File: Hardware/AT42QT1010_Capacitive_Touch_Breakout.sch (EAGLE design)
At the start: 28 parts, among them Q1 NPN, U1 AT42QT1010SOT23

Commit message: Ready for red board review
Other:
- note added: "10"
- note removed: "02"
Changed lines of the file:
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@@
 <setting verticaltext="up"/>
 </settings>
-<grid distance="0.1" unitdist="inch" unit="inch" style="lines" multiple="1" display="yes" altdistance="0.01" altunitdist="inch" altunit="inch"/>
+<grid distance="0.1" unitdist="inch" unit="inch" style="lines" multiple="1" display="no" altdistance="0.01" altunitdist="inch" altunit="inch"/>
 <layers>
 <layer number="1" name="Top" color="4" fill="1" visible="no" active="no"/>
@@
 <plain>
 <text x="172.212" y="7.62" size="3.81" layer="94">Shawn Hymel</text>
-<text x="239.014" y="6.604" size="3.81" layer="94">02</text>
+<text x="239.014" y="6.604" size="3.81" layer="94">10</text>
 <wire x1="101.6" y1="185.42" x2="101.6" y2="139.7" width="0.1524" layer="97" style="longdash"/>
 <wire x1="101.6" y1="139.7" x2="101.6" y2="76.2" width="0.1524" layer="97" style="longdash"/>

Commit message: Replaced old IC package with new smaller package
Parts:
- U1: value AT42QT1010SOT23 -> AT42QT1010UDFN; device SparkFun-DigitalIC:AT42QT1010SOT23 -> Testing:AT42QT1010UDFN
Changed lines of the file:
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@@
 <?xml version="1.0" encoding="utf-8"?>
 <!DOCTYPE eagle SYSTEM "eagle.dtd">
-<eagle version="6.0">
+<eagle version="7.7.0">
 <drawing>
 <settings>
@@
 <layer number="54" name="bGND_GNDA" color="1" fill="9" visible="no" active="no"/>
 <layer number="56" name="wert" color="7" fill="1" visible="no" active="no"/>
+<layer number="57" name="tCAD" color="7" fill="1" visible="no" active="no"/>
+<layer number="59" name="tCarbon" color="7" fill="1" visible="no" active="no"/>
+<layer number="60" name="bCarbon" color="7" fill="1" visible="no" active="no"/>
+<layer number="90" name="Modules" color="5" fill="1" visible="no" active="no"/>
 <layer number="91" name="Nets" color="2" fill="1" visible="yes" active="yes"/>
 <layer number="92" name="Busses" color="1" fill="1" visible="yes" active="yes"/>
@@
 <layer number="97" name="Info" color="7" fill="1" visible="yes" active="yes"/>
 <layer number="98" name="Guide" color="6" fill="1" visible="yes" active="yes"/>
+<layer number="99" name="SpiceOrder" color="7" fill="1" visible="yes" active="yes"/>
 <layer number="100" name="Muster" color="7" fill="1" visible="no" active="no"/>
 <layer number="101" name="Patch_Top" color="12" fill="4" visible="yes" active="yes"/>
@@
 <layer number="108" name="tplace-old" color="10" fill="1" visible="yes" active="yes"/>
 <layer number="109" name="ref-old" color="11" fill="1" visible="yes" active="yes"/>
+<layer number="110" name="fp0" color="7" fill="1" visible="yes" active="yes"/>
+<layer number="111" name="LPC17xx" color="7" fill="1" visible="yes" active="yes"/>
+<layer number="112" name="tSilk" color="7" fill="1" visible="yes" active="yes"/>
+<layer number="113" name="IDFDebug" color="4" fill="1" visible="yes" active="yes"/>
+<layer number="114" name="Badge_Outline" color="11" fill="1" visible="no" active="no"/>
+<layer number="115" name="ReferenceISLANDS" color="7" fill="1" visible="yes" active="yes"/>
 <layer number="116" name="Patch_BOT" color="9" fill="4" visible="yes" active="yes"/>
+<layer number="118" name="Rect_Pads" color="7" fill="1" visible="yes" active="yes"/>
 <layer number="121" name="_tsilk" color="7" fill="1" visible="yes" active="yes"/>
 <layer number="122" name="_bsilk" color="7" fill="1" visible="yes" active="yes"/>
+<layer number="123" name="tTestmark" color="7" fill="1" visible="yes" active="yes"/>
+<layer number="124" name="bTestmark" color="7" fill="1" visible="yes" active="yes"/>
 <layer number="125" name="_tNames" color="7" fill="1" visible="yes" active="yes"/>
+<layer number="126" name="_bNames" color="7" fill="1" visible="yes" active="yes"/>
+<layer number="127" name="_tValues" color="7" fill="1" visible="yes" active="yes"/>
+<layer number="128" name="_bValues" color="7" fill="1" visible="yes" active="yes"/>
+<layer number="129" name="Mask" color="7" fill="1" visible="yes" active="yes"/>
+<layer number="131" name="tAdjust" color="7" fill="1" visible="yes" active="yes"/>
+<layer number="132" name="bAdjust" color="7" fill="1" visible="yes" active="yes"/>
 <layer number="144" name="Drill_legend" color="7" fill="1" visible="yes" active="yes"/>
+<layer number="150" name="Notes" color="7" fill="1" visible="yes" active="yes"/>
 <layer number="151" name="HeatSink" color="7" fill="1" visible="yes" active="yes"/>
+<layer number="152" name="_bDocu" color="7" fill="1" visible="yes" active="yes"/>
+<layer number="153" name="FabDoc1" color="7" fill="1" visible="yes" active="yes"/>
+<layer number="154" name="FabDoc2" color="7" fill="1" visible="yes" active="yes"/>
+<layer number="155" name="FabDoc3" color="7" fill="1" visible="yes" active="yes"/>
 <layer number="199" name="Contour" color="7" fill="1" visible="yes" active="yes"/>
 <layer number="200" name="200bmp" color="1" fill="10" visible="yes" active="yes"/>
@@
 <layer number="223" name="223bmp" color="24" fill="1" visible="no" active="no"/>
 <layer number="224" name="224bmp" color="25" fill="1" visible="no" active="no"/>
+<layer number="225" name="225bmp" color="7" fill="1" visible="yes" active="yes"/>
+<layer number="226" name="226bmp" color="7" fill="1" visible="yes" active="yes"/>
+<layer number="227" name="227bmp" color="7" fill="1" visible="yes" active="yes"/>
+<layer number="228" name="228bmp" color="7" fill="1" visible="yes" active="yes"/>
+<layer number="229" name="229bmp" color="7" fill="1" visible="yes" active="yes"/>
+<layer number="230" name="230bmp" color="7" fill="1" visible="yes" active="yes"/>
+<layer number="231" name="231bmp" color="7" fill="1" visible="yes" active="yes"/>
+<layer number="232" name="Eagle3D_PG2" color="7" fill="1" visible="yes" active="yes"/>
+<layer number="233" name="Eagle3D_PG3" color="7" fill="1" visible="yes" active="yes"/>
+<layer number="248" name="Housing" color="7" fill="1" visible="yes" active="yes"/>
+<layer number="249" name="Edge" color="7" fill="1" visible="yes" active="yes"/>
 <layer number="250" name="Descript" color="3" fill="1" visible="no" active="no"/>
 <layer number="251" name="SMDround" color="12" fill="11" visible="no" active="no"/>
 <layer number="254" name="cooling" color="7" fill="1" visible="yes" active="yes"/>
+<layer number="255" name="routoute" color="7" fill="1" visible="yes" active="yes"/>
 </layers>
 <schematic xreflabel="%F%N/%S.%C%R" xrefpart="/%S.%C%R">
@@
 </classes>
 <parts>
-<part name="U1" library="SparkFun-DigitalIC" deviceset="AT42QT1010" device="SOT23"/>
+<part name="U1" library="Testing" deviceset="AT42QT1010" device="UDFN"/>
 <part name="FRAME1" library="SparkFun-Aesthetics" deviceset="FRAME-LETTER" device=""/>
 <part name="LOGO2" library="SparkFun-Aesthetics" deviceset="OSHW-LOGO" device="S"/>

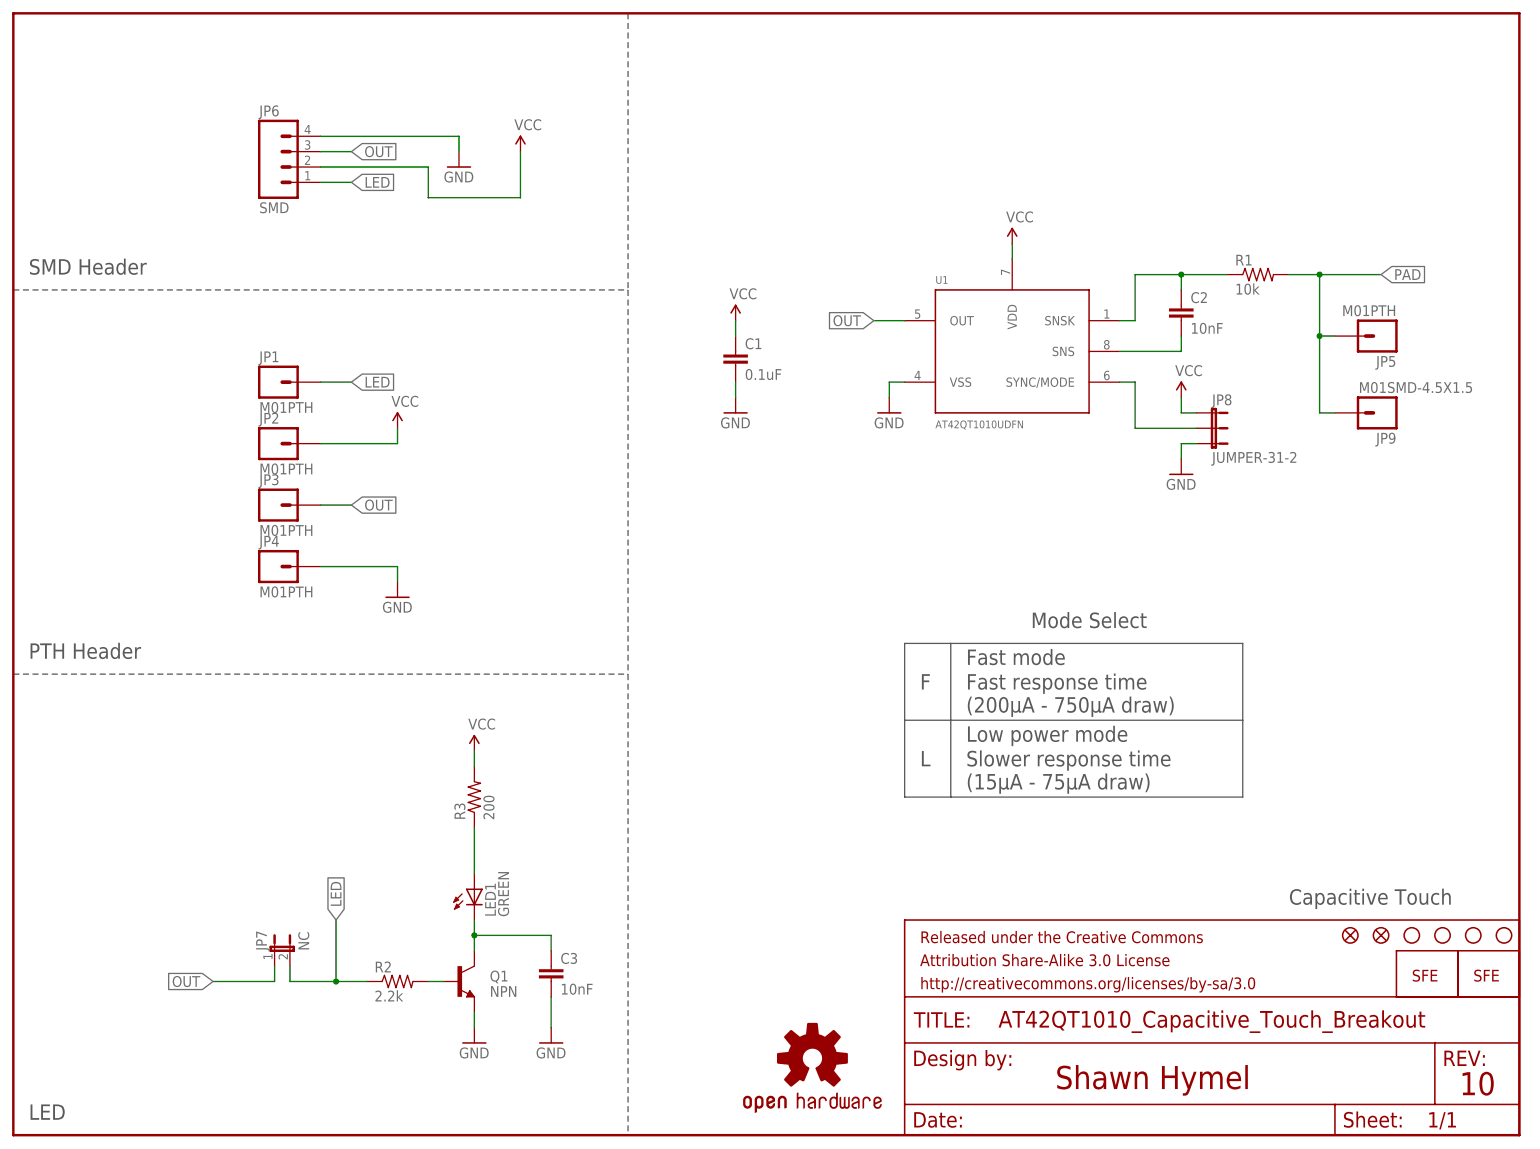
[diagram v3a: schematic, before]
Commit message: Orphans, Schematic changes
Adjusted some traces, updated CC frame, added VCC range, updated jumpers
to a more current package, added fiducials to underside, added Sparkfun
label to schematic.
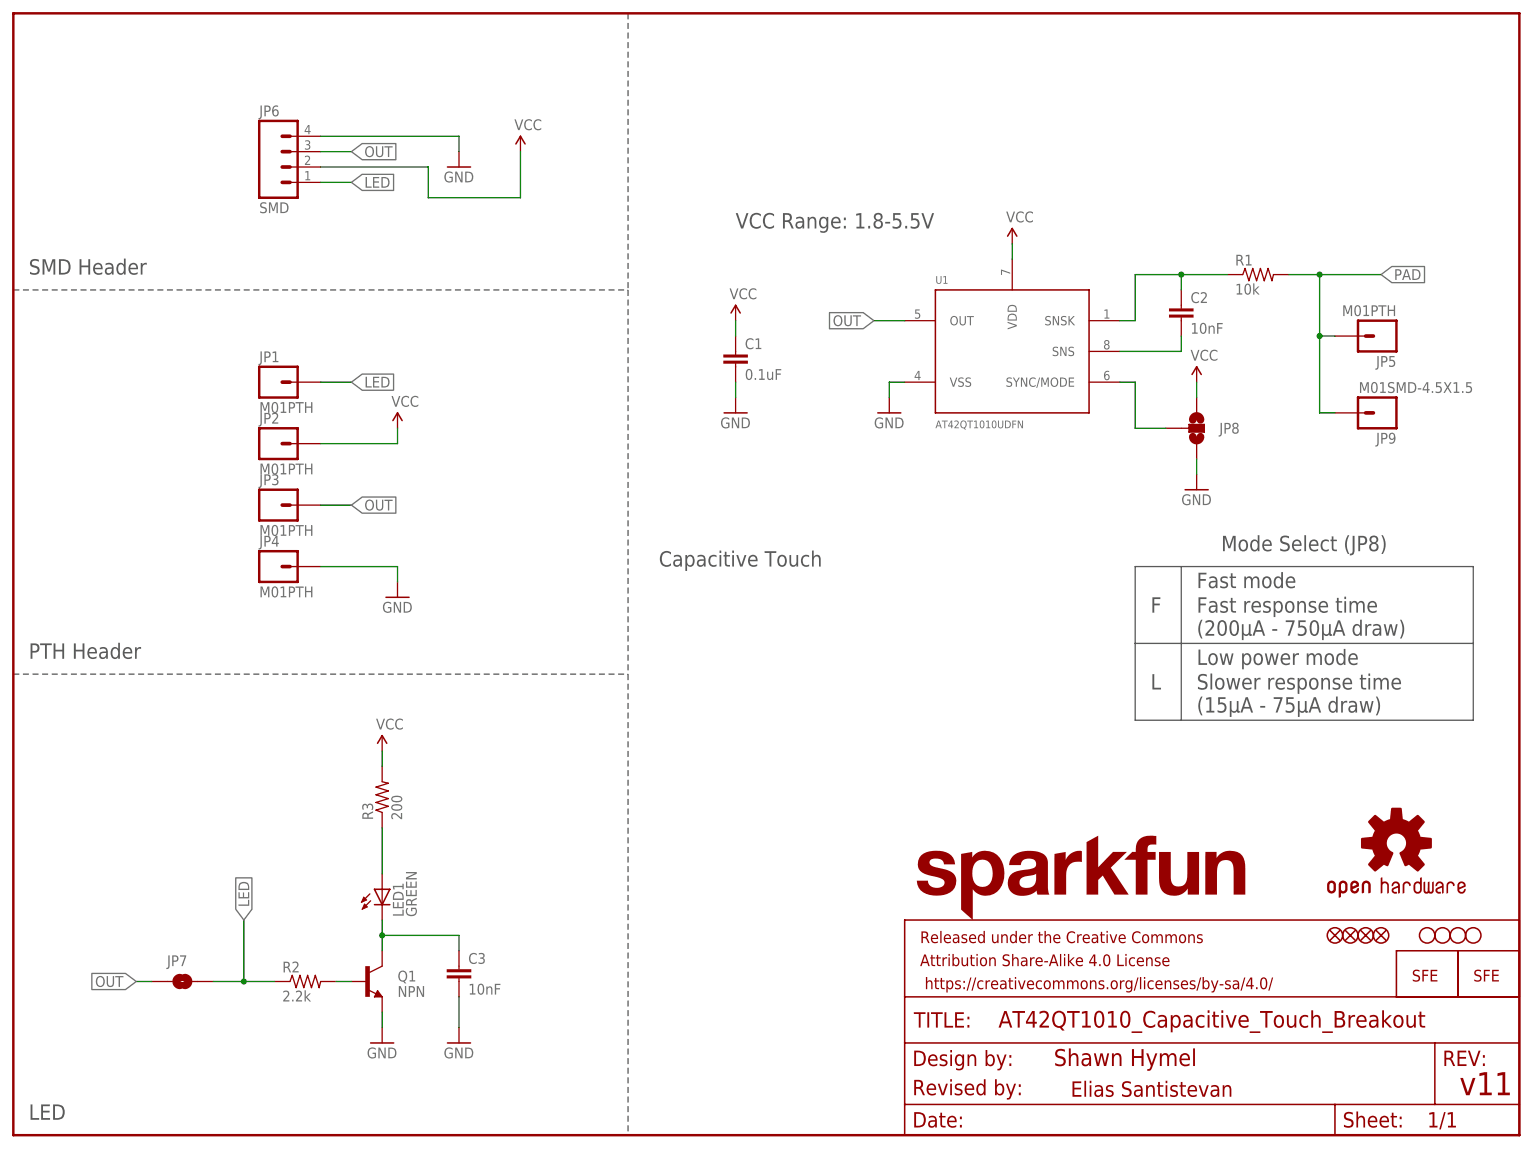
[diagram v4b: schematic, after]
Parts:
- added FID3, FID4: FIDUCIAL1X2, SparkFun-Aesthetics:FIDUCIAL1X2
- added LOGO4: SFE_LOGO_NAME.1_INCH, SparkFun-Aesthetics:SFE_LOGO_NAME.1_INCH
- JP7: value NC -> JUMPER-SMT_2_NO_SILK; device SparkFun-Passives:JUMPER-2SMD-NC -> SparkFun-Jumpers:JUMPER-SMT_2_NO_SILK
- JP8: value JUMPER-31-2 -> JUMPER-SMT_3_NO_SILK; device SparkFun-Passives:JUMPER-31-2 -> SparkFun-Jumpers:JUMPER-SMT_3_NO_SILK
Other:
- note added: "Elias Santistevan"
- note added: "Mode Select (JP8)"
- note added: "Revised by:"
- note added: "VCC Range: 1.8-5.5V"
- note added: "v11"
- note removed: "10"
- note removed: "Mode Select"
- moved on the sheet: C3, LED1, Q1, R2, R3

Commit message: Silk, 0603 packages, flipped header
Fixed some redundant silk, replaced all 0603 packages with newer
versions, and flipped the 4 pin header to align with the PTH headers on
the schematic.
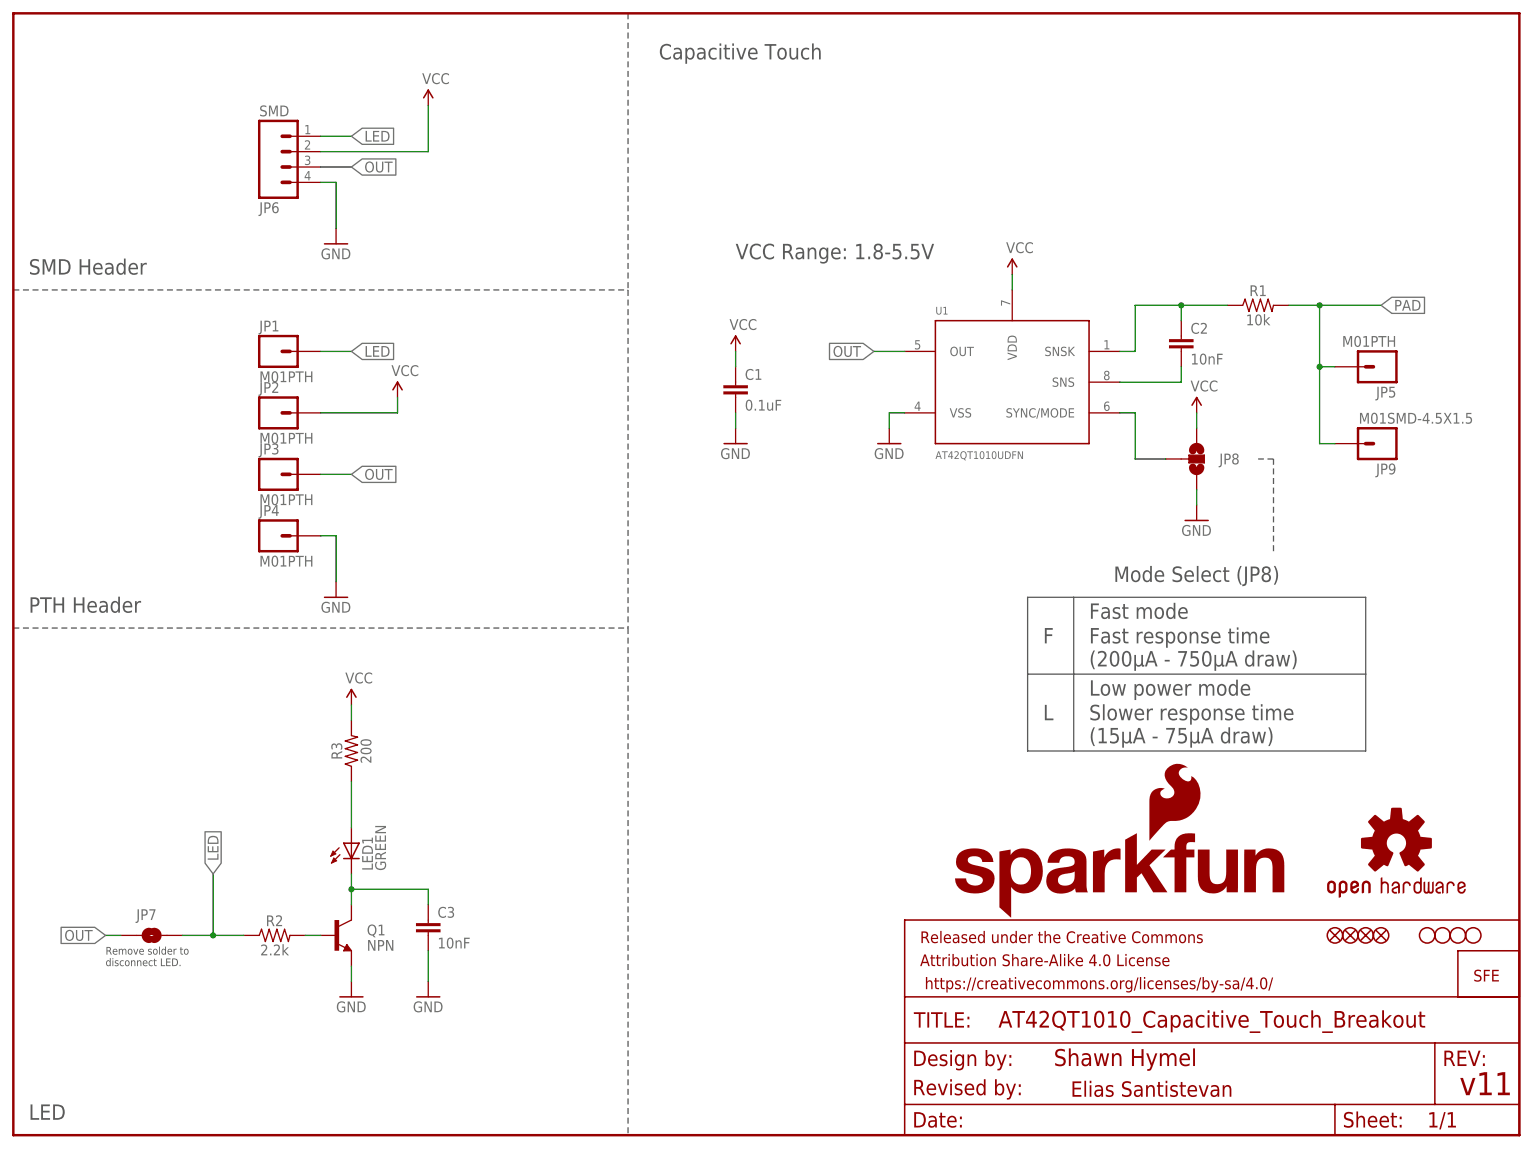
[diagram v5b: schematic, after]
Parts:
- removed LOGO1: LOGO-SFENEW, SparkFun-Aesthetics:LOGO-SFENEW
- removed LOGO4: SFE_LOGO_NAME.1_INCH, SparkFun-Aesthetics:SFE_LOGO_NAME.1_INCH
- added LOGO5: SFE_LOGO_NAME_WEB, SparkFun-Aesthetics:SFE_LOGO_NAME_WEB
- C1: device SparkFun-Capacitors:CAP0603-CAP -> SparkFun-Capacitors:0.1UF-0603-25V-(+80/-20%)
- C2, C3: device SparkFun-Capacitors:CAP0603-CAP -> SparkFun-Capacitors:10NF-0603-50V-10%
- R1: device SparkFun-Resistors:RESISTOR0603 -> SparkFun-Resistors:10KOHM-0603-1/10W-1%
- R2: device SparkFun-Resistors:RESISTOR0603 -> SparkFun-Resistors:2.2KOHM-0603-1/10W-1%
- R3: device SparkFun-Resistors:RESISTOR0603 -> SparkFun-Resistors:200OHM-0603-1/10W-1%
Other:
- note added: "Remove solder to disconnect LED."
- moved on the sheet: C1, C2, C3, JP1, JP2, JP3, JP4, JP5, JP6, JP7, JP8, JP9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
